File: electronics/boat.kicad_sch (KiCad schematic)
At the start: 0 parts

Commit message: cleaned code and folder structure, previous commit bug still remains
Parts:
- added C5, C6, C8: 0.1uF, symbol ME218_BaseLib:Cap
- added C7: 10uF, symbol ME218_BaseLib:Cap
- added D2: LED, symbol Device:LED
- added J2: UART1, symbol Connector:Conn_01x02_Socket
- added PRG2: MPLAB_Snap, symbol ME218_BaseLib:MPLAB_Snap
- added R4: 1K, symbol ME218_BaseLib:Res2
- added R5: 10K, symbol ME218_BaseLib:Res2
- added R7: 220, symbol Device:R
- added SW1: Reset, symbol ME218_BaseLib:SW-PB
- added U2: PIC32MX170F256B, symbol ME218_BaseLib:PIC32MX170F256B
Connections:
- new net: PRG2.1 (~{MCLR}/Vpp), R4.1, U2.1 (~{MCLR})
- new net: D2.2 (A), U2.14 (PGED3/5VT/RB5)
- new net: C7.2, U2.20 (Vcap)
- new net: PRG2.4 (PGData), U2.4 (PGED1/RB0)
- new net: PRG2.5 (PGClk), U2.5 (PGEC1/RB1)
- new net: C8.1, R4.2, R5.1, SW1.1
- new net: D2.1 (K), R7.1
- new net +3V3: C5.1, C6.2, PRG2.2 (Vdd), R5.2, U2.13 (Vdd), U2.28 (AVdd)
- new net GND: C5.2, C6.1, C7.1, C8.2, PRG2.3 (Vss), R7.2, SW1.2, U2.19 (Vss), U2.27 (AVss), U2.8 (Vss)
- new net INVERT: U2.26 (RB15)
- new net RX: J2.1 (Pin_1), U2.16 (5VT/RB7)
- new net TRIGGER: U2.25 (RB14)
- new net TX: J2.2 (Pin_2), U2.15 (PGEC3/5VT/RB6)
- new net UART2RX: U2.17 (5VT/RB8)
- new net UART2TX: U2.18 (PGED2/5VT/RB9)
- no-connect marks 0 -> 12
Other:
- note added: "for programming"
- title: (none) -> Boat Electronics

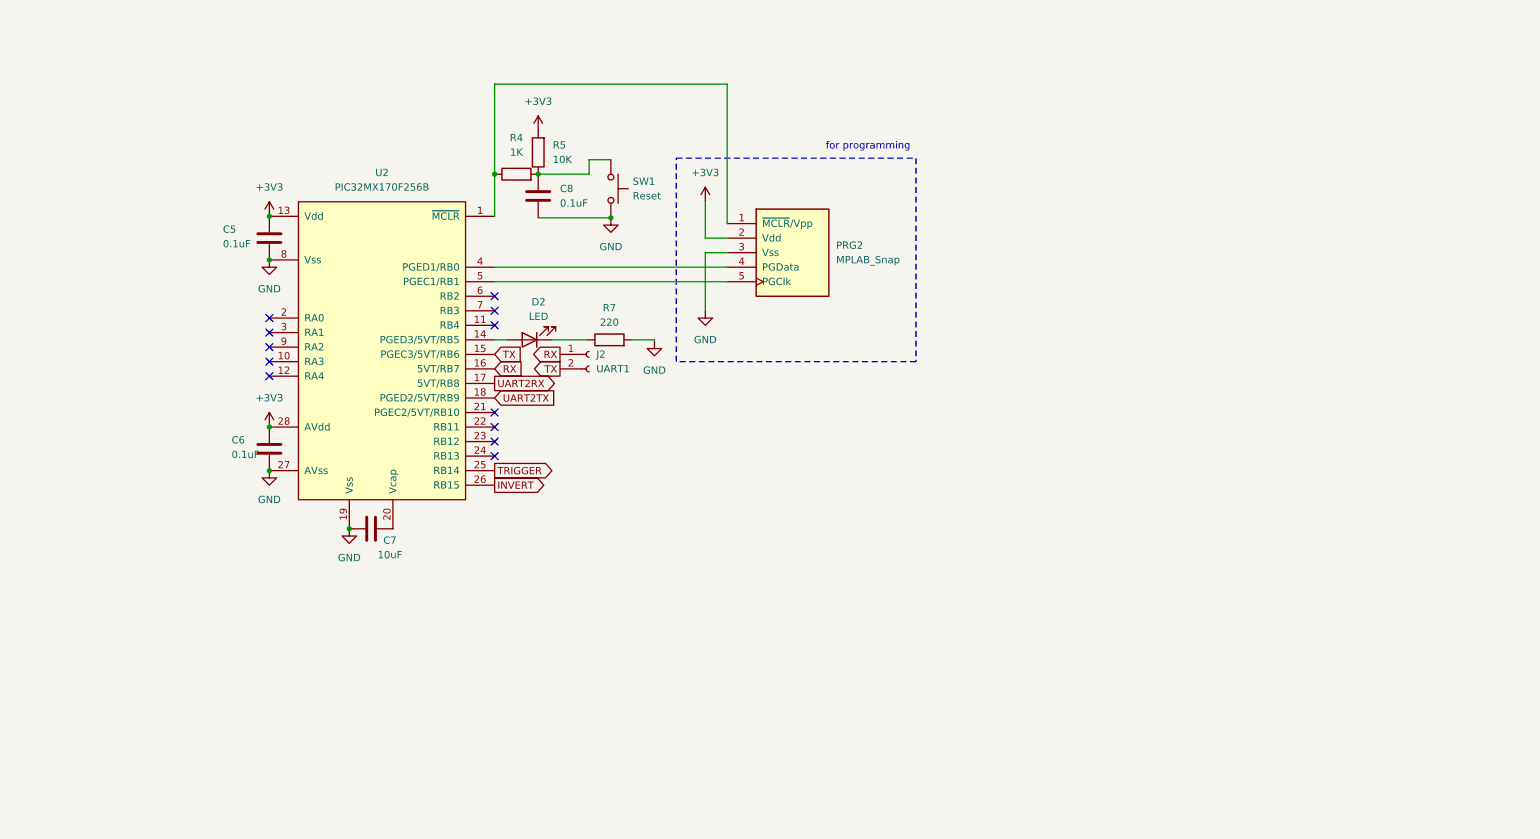
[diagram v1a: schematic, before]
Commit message: schematic progress with all current priority components and pin selections
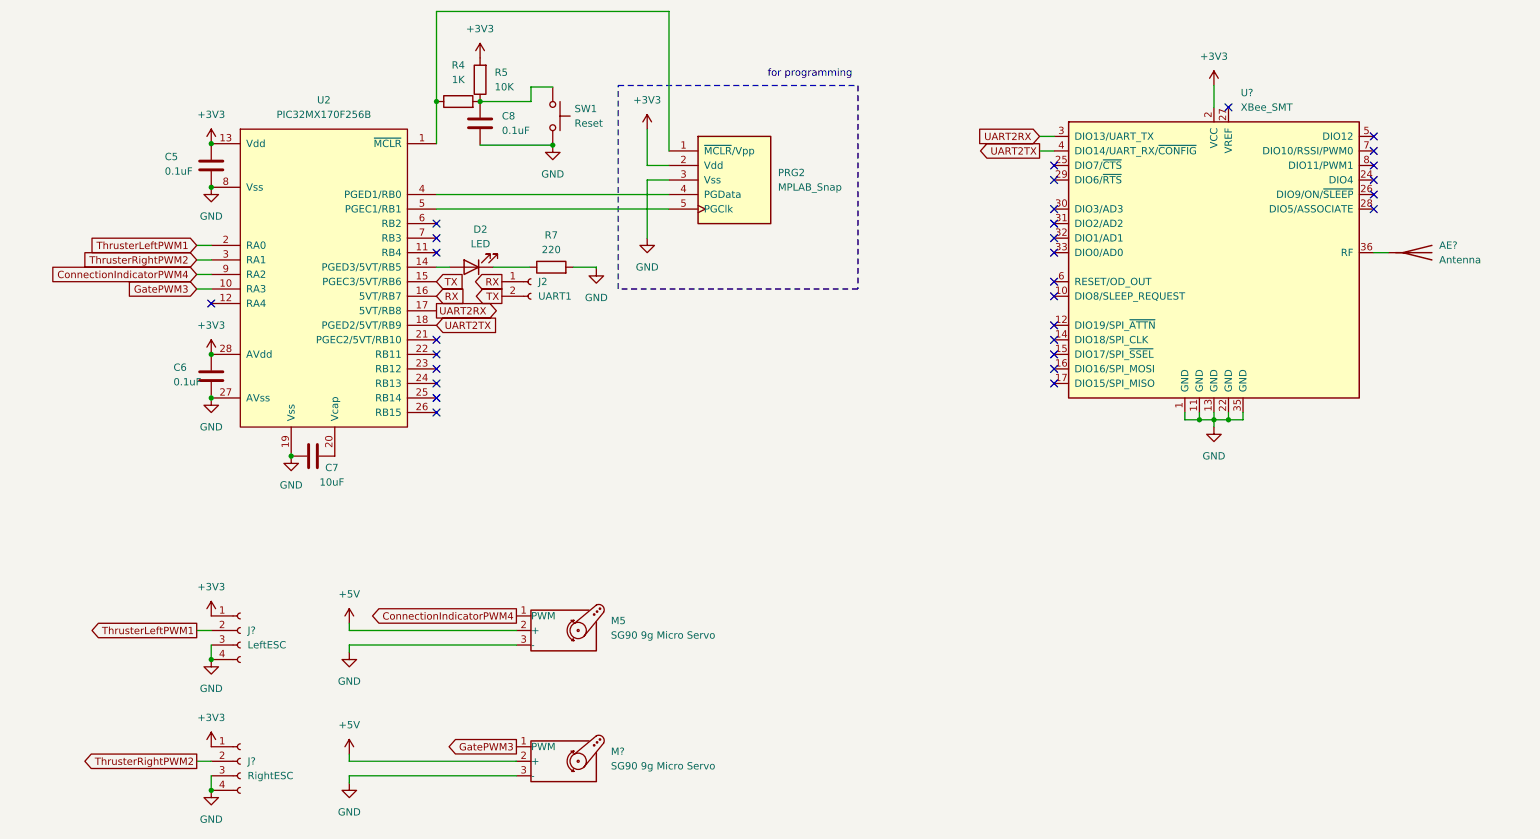
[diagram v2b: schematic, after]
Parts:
- added AE?: Antenna, symbol Device:Antenna
- added J?: RightESC, symbol Connector:Conn_01x04_Socket
- added J?: LeftESC, symbol Connector:Conn_01x04_Socket
- added M5, M?: SG90 9g Micro Servo, symbol ME218_BaseLib:Motor_Servo
- added U?: XBee_SMT, RF_Module:Digi_XBee_SMT, symbol RF_ZigBee:XBee_SMT
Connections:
- net +3V3: now also J?.1 (Pin_1), J?.1 (Pin_1), U?.2 (VCC)
- net GND: now also J?.3 (Pin_3), J?.3 (Pin_3), J?.4 (Pin_4), J?.4 (Pin_4), M5.3 (-), M?.3 (-), U?.1 (GND), U?.11 (GND), U?.13 (GND), U?.22 (GND), U?.35 (GND)
- net UART2RX: now also U?.3 (DIO13/UART_TX)
- net UART2TX: now also U?.4 (DIO14/UART_RX/~{CONFIG})
- net GatePWM3: now reaches U2.10 (RA3)
- net GatePWM3: now also M?.1 (PWM)
- net ThrusterLeftPWM1: now reaches U2.2 (RA0)
- net ThrusterLeftPWM1: now also J?.2 (Pin_2)
- net ThrusterRightPWM2: now reaches U2.3 (RA1)
- net ThrusterRightPWM2: now also J?.2 (Pin_2)
- net ConnectionIndicatorPWM4: now reaches U2.9 (RA2)
- net ConnectionIndicatorPWM4: now also M5.1 (PWM)
- net INVERT: no longer names the net of U2.26 (RB15)
- net TRIGGER: no longer names the net of U2.25 (RB14)
- new net: AE?.1 (A), U?.36 (RF)
- new net +5V: M5.2 (+), M?.2 (+)
- no-connect marks 12 -> 30
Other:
- moved on the sheet: C5, C6, C7, C8, D2, J2, PRG2, R4, R5, R7, SW1, U2

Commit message: update schematic to reflect motor voltage
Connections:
- net +3V3: no longer J?.1 (Pin_1), J?.1 (Pin_1)
- new net +14V: J?.1 (Pin_1), J?.1 (Pin_1)
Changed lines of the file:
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@@
-	(symbol
-		(lib_id "power:+3V3")
-		(at 50.8 153.67 0)
-		(unit 1)
-		(exclude_from_sim no)
-		(in_bom yes)
-		(on_board yes)
-		(dnp no)
-		(fields_autoplaced yes)
-		(property "Reference" "#PWR023"
-			(at 50.8 157.48 0)
-			(effects
-				(font
-					(size 1.27 1.27)
-				)
-				(hide yes)
-			)
-		)
-		(property "Value" "+3V3"
-			(at 50.8 148.59 0)
-			(effects
-				(font
-					(size 1.27 1.27)
-				)
-			)
-		)
-		(property "Footprint" ""
-			(at 50.8 153.67 0)
-			(effects
-				(font
-					(size 1.27 1.27)
-				)
-				(hide yes)
-			)
-		)
-		(property "Datasheet" ""
-			(at 50.8 153.67 0)
-			(effects
-				(font
-					(size 1.27 1.27)
-				)
-				(hide yes)
-			)
-		)
-		(property "Description" "Power symbol creates a global label with name \"+3V3\""
-			(at 50.8 153.67 0)
-			(effects
-				(font
-					(size 1.27 1.27)
-				)
-				(hide yes)
-			)
-		)
-		(pin "1"
-		)
-		(instances
-			(project "boatElectronics"
-				(path "/bd24c4db-4e36-4117-bd4f-5228ef241da9/dae846a3-5621-40b2-bbb5-71c56d87180c"
-					(reference "#PWR023")
-					(unit 1)
-				)
-			)
-		)
-	)
 	(symbol
 		(lib_id "power:+3V3")
@@
 	)
 	(symbol
+		(lib_id "power:+12V")
+		(at 50.8 130.81 0)
+		(unit 1)
+		(exclude_from_sim no)
+		(in_bom yes)
+		(on_board yes)
+		(dnp no)
+		(fields_autoplaced yes)
+		(property "Reference" "#PWR022"
+			(at 50.8 134.62 0)
+			(effects
+				(font
+					(size 1.27 1.27)
+				)
+				(hide yes)
+			)
+		)
+		(property "Value" "+14V"
+			(at 50.8 125.73 0)
+			(effects
+				(font
+					(size 1.27 1.27)
+				)
+			)
+		)
+		(property "Footprint" ""
+			(at 50.8 130.81 0)
+			(effects
+				(font
+					(size 1.27 1.27)
+				)
+				(hide yes)
+			)
+		)
+		(property "Datasheet" ""
+			(at 50.8 130.81 0)
+			(effects
+				(font
+					(size 1.27 1.27)
+				)
+				(hide yes)
+			)
+		)
+		(property "Description" "Power symbol creates a global label with name \"+12V\""
+			(at 50.8 130.81 0)
+			(effects
+				(font
+					(size 1.27 1.27)
+				)
+				(hide yes)
+			)
+		)
+		(pin "1"
+		)
+		(instances
+			(project ""
+				(path "/bd24c4db-4e36-4117-bd4f-5228ef241da9/dae846a3-5621-40b2-bbb5-71c56d87180c"
+					(reference "#PWR022")
+					(unit 1)
+				)
+			)
+		)
+	)
+	(symbol
+		(lib_id "power:+12V")
+		(at 50.8 153.67 0)
+		(unit 1)
+		(exclude_from_sim no)
+		(in_bom yes)
+		(on_board yes)
+		(dnp no)
+		(fields_autoplaced yes)
+		(property "Reference" "#PWR023"
+			(at 50.8 157.48 0)
+			(effects
+				(font
+					(size 1.27 1.27)
+				)
+				(hide yes)
+			)
+		)
+		(property "Value" "+14V"
+			(at 50.8 148.59 0)
+			(effects
+				(font
+					(size 1.27 1.27)
+				)
+			)
+		)
+		(property "Footprint" ""
+			(at 50.8 153.67 0)
+			(effects
+				(font
+					(size 1.27 1.27)
+				)
+				(hide yes)
+			)
+		)
+		(property "Datasheet" ""
+			(at 50.8 153.67 0)
+			(effects
+				(font
+					(size 1.27 1.27)
+				)
+				(hide yes)
+			)
+		)
+		(property "Description" "Power symbol creates a global label with name \"+12V\""
+			(at 50.8 153.67 0)
+			(effects
+				(font
+					(size 1.27 1.27)
+				)
+				(hide yes)
+			)
+		)
+		(pin "1"
+		)
+		(instances
+			(project "boatElectronics"
+				(path "/bd24c4db-4e36-4117-bd4f-5228ef241da9/dae846a3-5621-40b2-bbb5-71c56d87180c"
+					(reference "#PWR023")
+					(unit 1)
+				)
+			)
+		)
+	)
+	(symbol
 		(lib_id "power:+3V3")
 		(at 74.93 132.08 0)
@@
 					(unit 1)
 				)
-			)
-		)
-	)
-	(symbol
-		(lib_id "power:+3V3")
-		(at 50.8 130.81 0)
-		(unit 1)
-		(exclude_from_sim no)
-		(in_bom yes)
-		(on_board yes)
-		(dnp no)
-		(fields_autoplaced yes)
-		(property "Reference" "#PWR022"
-			(at 50.8 134.62 0)
-			(effects
-				(font
-					(size 1.27 1.27)
-				)
-				(hide yes)
-			)
-		)
-		(property "Value" "+3V3"
-			(at 50.8 125.73 0)
-			(effects
-				(font
-					(size 1.27 1.27)
-				)
-			)
-		)
-		(property "Footprint" ""
-			(at 50.8 130.81 0)
-			(effects
-				(font
-					(size 1.27 1.27)
-				)
-				(hide yes)
-			)
-		)
-		(property "Datasheet" ""
-			(at 50.8 130.81 0)
-			(effects
-				(font
-					(size 1.27 1.27)
-				)
-				(hide yes)
-			)
-		)
-		(property "Description" "Power symbol creates a global label with name \"+3V3\""
-			(at 50.8 130.81 0)
-			(effects
-				(font
-					(size 1.27 1.27)
-				)
-				(hide yes)
-			)
-		)
-		(pin "1"
-		)
-		(instances
-			(project "boatElectronics"
-				(path "/bd24c4db-4e36-4117-bd4f-5228ef241da9/dae846a3-5621-40b2-bbb5-71c56d87180c"
-					(reference "#PWR022")
-					(unit 1)
-				)

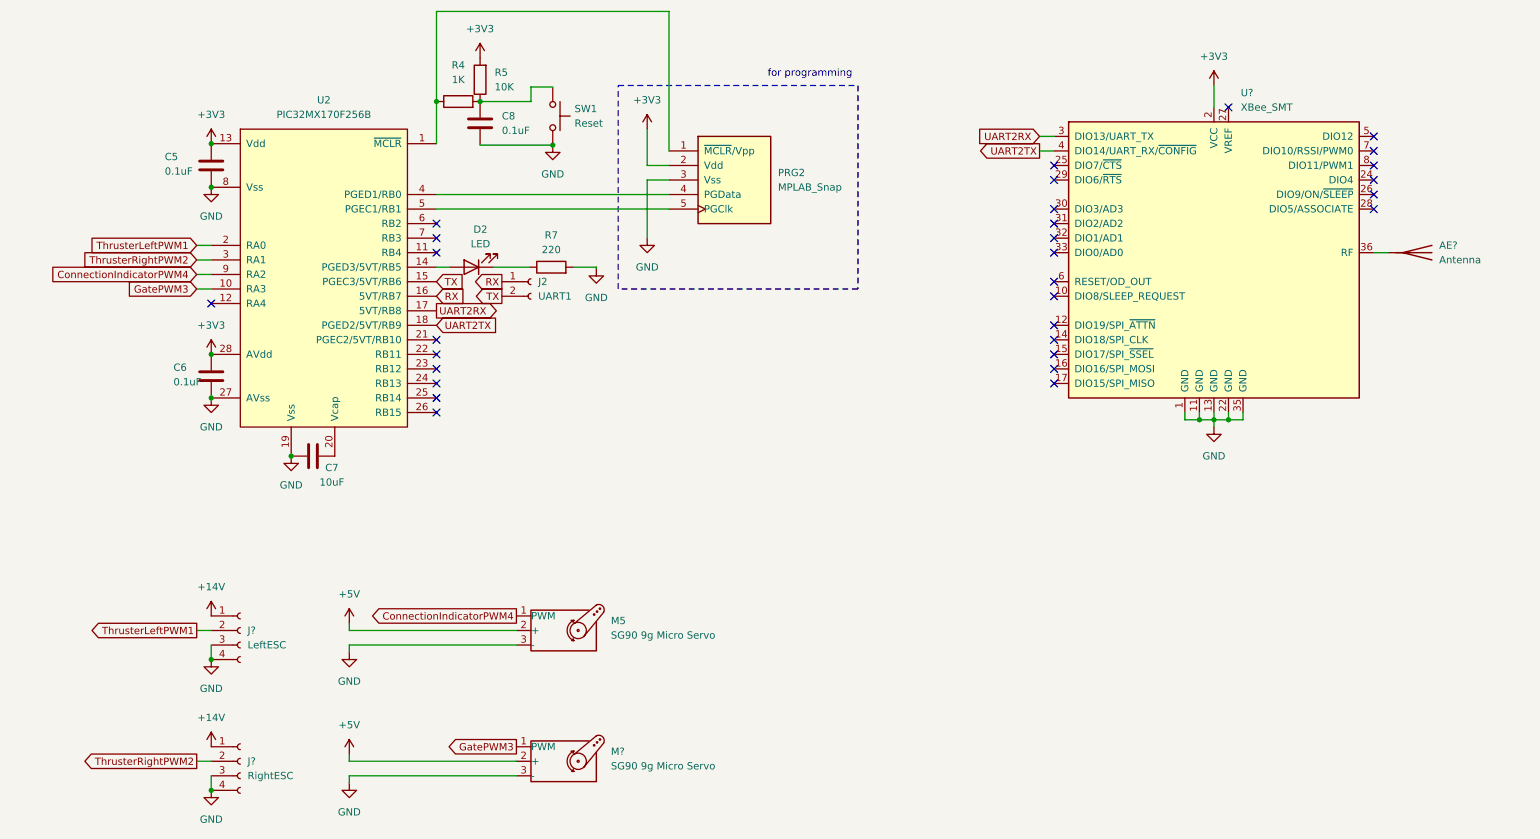
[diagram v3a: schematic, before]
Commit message: added water pump to RA4
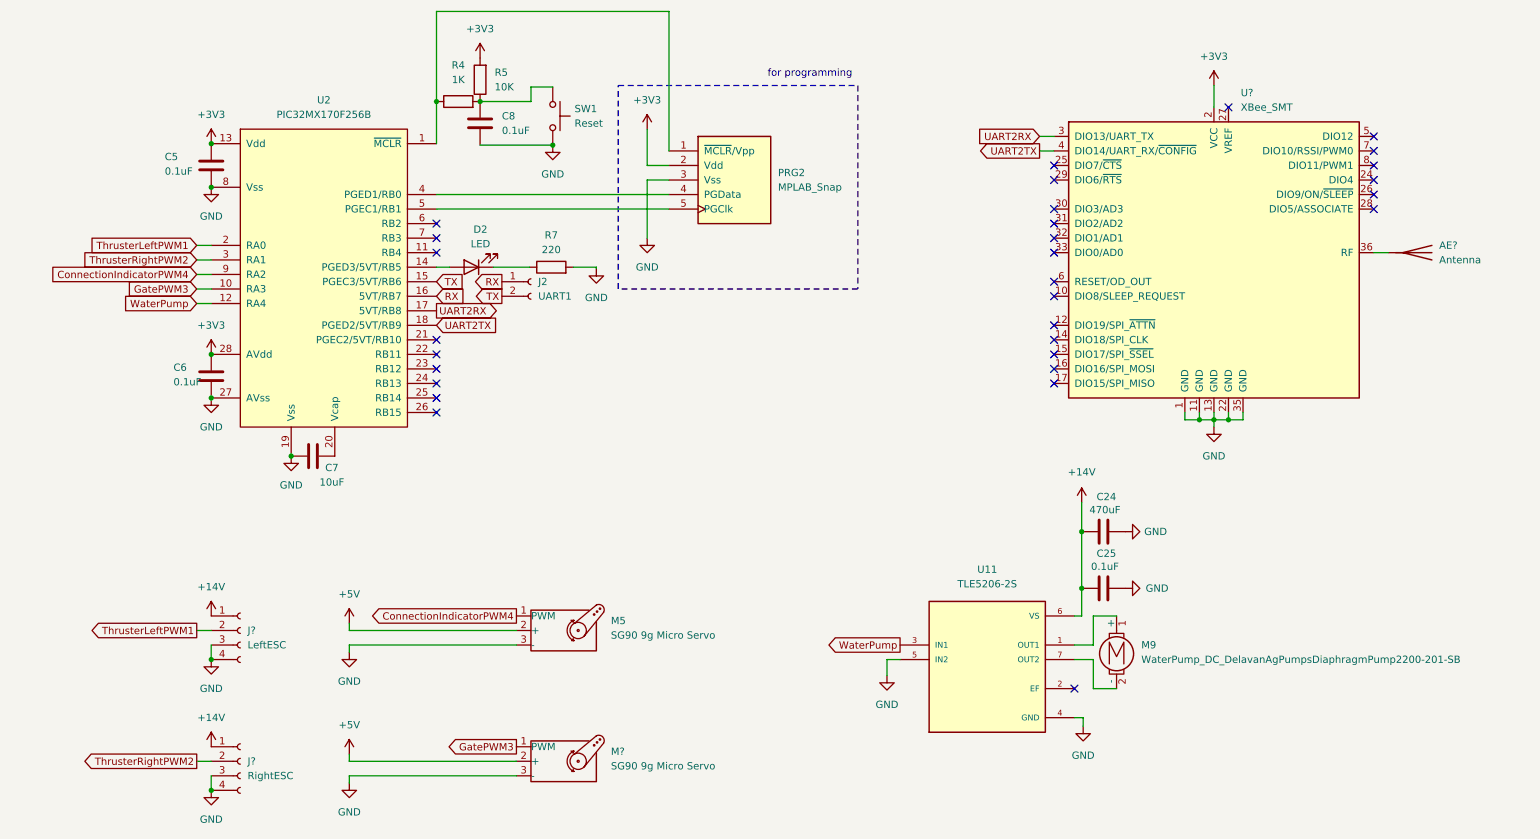
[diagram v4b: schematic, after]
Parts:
- added C24: 470uF, symbol ME218_BaseLib:Cap
- added C25: 0.1uF, symbol ME218_BaseLib:Cap
- added M9: WaterPump_DC_DelavanAgPumpsDiaphragmPump2200-201-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, symbol Motor:Motor_DC_ALT
- added U11: TLE5206-2S, TLE5206-2S:TO127P1000X440X1730-7, symbol TLE5206-2S:TLE5206-2S
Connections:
- net +14V: now also C24.2, C25.2, U11.6 (VS)
- net GND: now also C24.1, C25.1, U11.4 (GND), U11.5 (IN2)
- net WaterPump: now reaches U2.12 (RA4)
- net WaterPump: now also U11.3 (IN1)
- new net: M9.1 (+), U11.1 (OUT1)
- new net: M9.2 (-), U11.7 (OUT2)

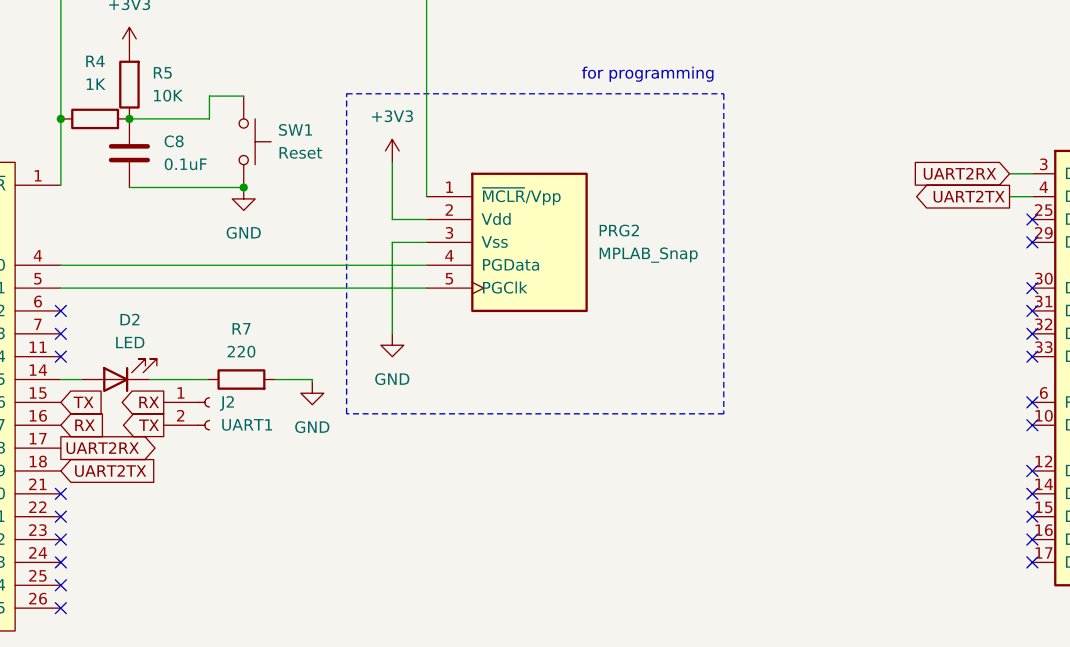
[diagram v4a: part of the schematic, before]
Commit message: added reference for xbee wiring
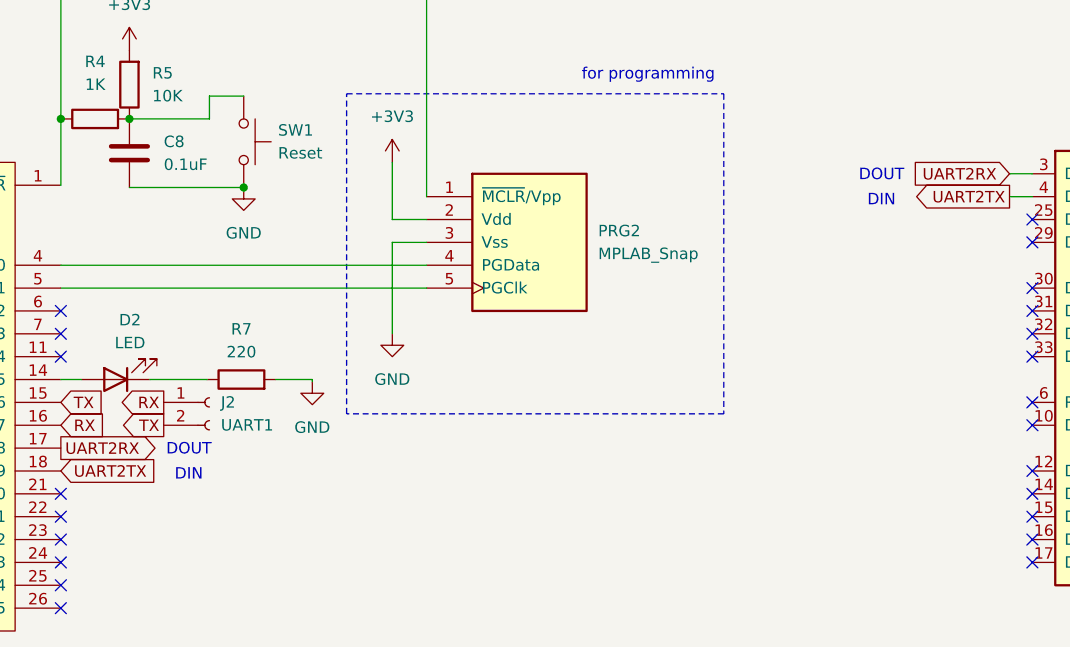
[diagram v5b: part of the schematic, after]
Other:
- note added: "DIN"
- note added: "DOUT"
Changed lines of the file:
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@@
+		)
+	)
+	(text "DOUT"
+		(exclude_from_sim no)
+		(at 104.394 77.724 0)
+		(effects
+			(font
+				(size 1.27 1.27)
+			)
 		)
 	)
@@
 		(effects
 			(font
+				(size 1.27 1.27)
+			)
+		)
+	)
+	(text "DIN"
+		(exclude_from_sim no)
+		(at 181.356 50.038 0)
+		(effects
+			(font
+				(size 1.27 1.27)
+			)
+		)
+	)
+	(text "DIN"
+		(exclude_from_sim no)
+		(at 104.394 80.518 0)
+		(effects
+			(font
+				(size 1.27 1.27)
+			)
+		)
+	)
+	(text "DOUT"
+		(exclude_from_sim no)
+		(at 181.356 47.244 0)
+		(effects
+			(font
